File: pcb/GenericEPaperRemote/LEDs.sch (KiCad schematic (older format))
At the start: 26 parts

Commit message: Added pullups for encoder and switch away from io0 to prevent boot to root-loader when rotary encoder pulls low)
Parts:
- D17, D18, D19, D20, D21, D22, D23, D24, D25, D26, D27, D28, D29: LCSC Url https://lcsc.com/product-detail/New-Arrivals_JST-Sales-Amer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 -> https://lcsc.com/product-detail/Light-Emitting-Diodes-LED_5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
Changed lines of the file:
@@
 F 2 "LED_SMD:LED_WS2812B_PLCC4_5.0x5.0mm_P3.2mm" H 1900 1850 50  0001 L TNN
 F 3 "https://cdn-shop.adafruit.com/datasheets/WS2812B.pdf" H 1950 1775 50  0001 L TNN
-F 4 "https://lcsc.com/product-detail/New-Arrivals_JST-Sales-America-S8B-PH-SM4-TB-LF-SN_C265121.html" H 1850 2150 50  0001 C CNN "LCSC Url"
+F 4 "https://lcsc.com/product-detail/Light-Emitting-Diodes-LED_5050-RGBIntegrated-Light-4Pin_C114586.html" H 1850 2150 50  0001 C CNN "LCSC Url"
 F 5 "WS2812B-B" H 1850 2150 50  0001 C CNN "MPN"
 	1    1850 2150
@@
 F 2 "LED_SMD:LED_WS2812B_PLCC4_5.0x5.0mm_P3.2mm" H 2500 1850 50  0001 L TNN
 F 3 "https://cdn-shop.adafruit.com/datasheets/WS2812B.pdf" H 2550 1775 50  0001 L TNN
-F 4 "https://lcsc.com/product-detail/New-Arrivals_JST-Sales-America-S8B-PH-SM4-TB-LF-SN_C265121.html" H 2450 2150 50  0001 C CNN "LCSC Url"
+F 4 "https://lcsc.com/product-detail/Light-Emitting-Diodes-LED_5050-RGBIntegrated-Light-4Pin_C114586.html" H 2450 2150 50  0001 C CNN "LCSC Url"
 F 5 "WS2812B-B" H 2450 2150 50  0001 C CNN "MPN"
 	1    2450 2150
@@
 F 2 "LED_SMD:LED_WS2812B_PLCC4_5.0x5.0mm_P3.2mm" H 3100 1850 50  0001 L TNN
 F 3 "https://cdn-shop.adafruit.com/datasheets/WS2812B.pdf" H 3150 1775 50  0001 L TNN
-F 4 "https://lcsc.com/product-detail/New-Arrivals_JST-Sales-America-S8B-PH-SM4-TB-LF-SN_C265121.html" H 3050 2150 50  0001 C CNN "LCSC Url"
+F 4 "https://lcsc.com/product-detail/Light-Emitting-Diodes-LED_5050-RGBIntegrated-Light-4Pin_C114586.html" H 3050 2150 50  0001 C CNN "LCSC Url"
 F 5 "WS2812B-B" H 3050 2150 50  0001 C CNN "MPN"
 	1    3050 2150
@@
 F 2 "LED_SMD:LED_WS2812B_PLCC4_5.0x5.0mm_P3.2mm" H 3700 1850 50  0001 L TNN
 F 3 "https://cdn-shop.adafruit.com/datasheets/WS2812B.pdf" H 3750 1775 50  0001 L TNN
-F 4 "https://lcsc.com/product-detail/New-Arrivals_JST-Sales-America-S8B-PH-SM4-TB-LF-SN_C265121.html" H 3650 2150 50  0001 C CNN "LCSC Url"
+F 4 "https://lcsc.com/product-detail/Light-Emitting-Diodes-LED_5050-RGBIntegrated-Light-4Pin_C114586.html" H 3650 2150 50  0001 C CNN "LCSC Url"
 F 5 "WS2812B-B" H 3650 2150 50  0001 C CNN "MPN"
 	1    3650 2150
@@
 F 2 "LED_SMD:LED_WS2812B_PLCC4_5.0x5.0mm_P3.2mm" H 4300 1850 50  0001 L TNN
 F 3 "https://cdn-shop.adafruit.com/datasheets/WS2812B.pdf" H 4350 1775 50  0001 L TNN
-F 4 "https://lcsc.com/product-detail/New-Arrivals_JST-Sales-America-S8B-PH-SM4-TB-LF-SN_C265121.html" H 4250 2150 50  0001 C CNN "LCSC Url"
+F 4 "https://lcsc.com/product-detail/Light-Emitting-Diodes-LED_5050-RGBIntegrated-Light-4Pin_C114586.html" H 4250 2150 50  0001 C CNN "LCSC Url"
 F 5 "WS2812B-B" H 4250 2150 50  0001 C CNN "MPN"
 	1    4250 2150
@@
 F 2 "LED_SMD:LED_WS2812B_PLCC4_5.0x5.0mm_P3.2mm" H 4900 1850 50  0001 L TNN
 F 3 "https://cdn-shop.adafruit.com/datasheets/WS2812B.pdf" H 4950 1775 50  0001 L TNN
-F 4 "https://lcsc.com/product-detail/New-Arrivals_JST-Sales-America-S8B-PH-SM4-TB-LF-SN_C265121.html" H 4850 2150 50  0001 C CNN "LCSC Url"
+F 4 "https://lcsc.com/product-detail/Light-Emitting-Diodes-LED_5050-RGBIntegrated-Light-4Pin_C114586.html" H 4850 2150 50  0001 C CNN "LCSC Url"
 F 5 "WS2812B-B" H 4850 2150 50  0001 C CNN "MPN"
 	1    4850 2150
@@
 F 2 "LED_SMD:LED_WS2812B_PLCC4_5.0x5.0mm_P3.2mm" H 5500 1850 50  0001 L TNN
 F 3 "https://cdn-shop.adafruit.com/datasheets/WS2812B.pdf" H 5550 1775 50  0001 L TNN
-F 4 "https://lcsc.com/product-detail/New-Arrivals_JST-Sales-America-S8B-PH-SM4-TB-LF-SN_C265121.html" H 5450 2150 50  0001 C CNN "LCSC Url"
+F 4 "https://lcsc.com/product-detail/Light-Emitting-Diodes-LED_5050-RGBIntegrated-Light-4Pin_C114586.html" H 5450 2150 50  0001 C CNN "LCSC Url"
 F 5 "WS2812B-B" H 5450 2150 50  0001 C CNN "MPN"
 	1    5450 2150
@@
 F 2 "LED_SMD:LED_WS2812B_PLCC4_5.0x5.0mm_P3.2mm" H 6100 1850 50  0001 L TNN
 F 3 "https://cdn-shop.adafruit.com/datasheets/WS2812B.pdf" H 6150 1775 50  0001 L TNN
-F 4 "https://lcsc.com/product-detail/New-Arrivals_JST-Sales-America-S8B-PH-SM4-TB-LF-SN_C265121.html" H 6050 2150 50  0001 C CNN "LCSC Url"
+F 4 "https://lcsc.com/product-detail/Light-Emitting-Diodes-LED_5050-RGBIntegrated-Light-4Pin_C114586.html" H 6050 2150 50  0001 C CNN "LCSC Url"
 F 5 "WS2812B-B" H 6050 2150 50  0001 C CNN "MPN"
 	1    6050 2150
@@
 F 2 "LED_SMD:LED_WS2812B_PLCC4_5.0x5.0mm_P3.2mm" H 6700 1850 50  0001 L TNN
 F 3 "https://cdn-shop.adafruit.com/datasheets/WS2812B.pdf" H 6750 1775 50  0001 L TNN
-F 4 "https://lcsc.com/product-detail/New-Arrivals_JST-Sales-America-S8B-PH-SM4-TB-LF-SN_C265121.html" H 6650 2150 50  0001 C CNN "LCSC Url"
+F 4 "https://lcsc.com/product-detail/Light-Emitting-Diodes-LED_5050-RGBIntegrated-Light-4Pin_C114586.html" H 6650 2150 50  0001 C CNN "LCSC Url"
 F 5 "WS2812B-B" H 6650 2150 50  0001 C CNN "MPN"
 	1    6650 2150
@@
 F 2 "LED_SMD:LED_WS2812B_PLCC4_5.0x5.0mm_P3.2mm" H 7300 1850 50  0001 L TNN
 F 3 "https://cdn-shop.adafruit.com/datasheets/WS2812B.pdf" H 7350 1775 50  0001 L TNN
-F 4 "https://lcsc.com/product-detail/New-Arrivals_JST-Sales-America-S8B-PH-SM4-TB-LF-SN_C265121.html" H 7250 2150 50  0001 C CNN "LCSC Url"
+F 4 "https://lcsc.com/product-detail/Light-Emitting-Diodes-LED_5050-RGBIntegrated-Light-4Pin_C114586.html" H 7250 2150 50  0001 C CNN "LCSC Url"
 F 5 "WS2812B-B" H 7250 2150 50  0001 C CNN "MPN"
 	1    7250 2150
@@
 F 2 "LED_SMD:LED_WS2812B_PLCC4_5.0x5.0mm_P3.2mm" H 7900 1850 50  0001 L TNN
 F 3 "https://cdn-shop.adafruit.com/datasheets/WS2812B.pdf" H 7950 1775 50  0001 L TNN
-F 4 "https://lcsc.com/product-detail/New-Arrivals_JST-Sales-America-S8B-PH-SM4-TB-LF-SN_C265121.html" H 7850 2150 50  0001 C CNN "LCSC Url"
+F 4 "https://lcsc.com/product-detail/Light-Emitting-Diodes-LED_5050-RGBIntegrated-Light-4Pin_C114586.html" H 7850 2150 50  0001 C CNN "LCSC Url"
 F 5 "WS2812B-B" H 7850 2150 50  0001 C CNN "MPN"
 	1    7850 2150
@@
 F 2 "LED_SMD:LED_WS2812B_PLCC4_5.0x5.0mm_P3.2mm" H 8500 1850 50  0001 L TNN
 F 3 "https://cdn-shop.adafruit.com/datasheets/WS2812B.pdf" H 8550 1775 50  0001 L TNN
-F 4 "https://lcsc.com/product-detail/New-Arrivals_JST-Sales-America-S8B-PH-SM4-TB-LF-SN_C265121.html" H 8450 2150 50  0001 C CNN "LCSC Url"
+F 4 "https://lcsc.com/product-detail/Light-Emitting-Diodes-LED_5050-RGBIntegrated-Light-4Pin_C114586.html" H 8450 2150 50  0001 C CNN "LCSC Url"
 F 5 "WS2812B-B" H 8450 2150 50  0001 C CNN "MPN"
 	1    8450 2150
@@
 F 2 "LED_SMD:LED_WS2812B_PLCC4_5.0x5.0mm_P3.2mm" H 9100 1850 50  0001 L TNN
 F 3 "https://cdn-shop.adafruit.com/datasheets/WS2812B.pdf" H 9150 1775 50  0001 L TNN
-F 4 "https://lcsc.com/product-detail/New-Arrivals_JST-Sales-America-S8B-PH-SM4-TB-LF-SN_C265121.html" H 9050 2150 50  0001 C CNN "LCSC Url"
+F 4 "https://lcsc.com/product-detail/Light-Emitting-Diodes-LED_5050-RGBIntegrated-Light-4Pin_C114586.html" H 9050 2150 50  0001 C CNN "LCSC Url"
 F 5 "WS2812B-B" H 9050 2150 50  0001 C CNN "MPN"
 	1    9050 2150

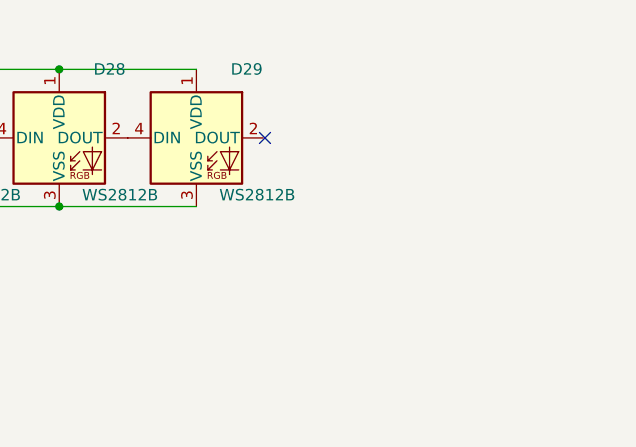
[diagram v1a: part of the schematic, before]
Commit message: added extension pins for ws2812b
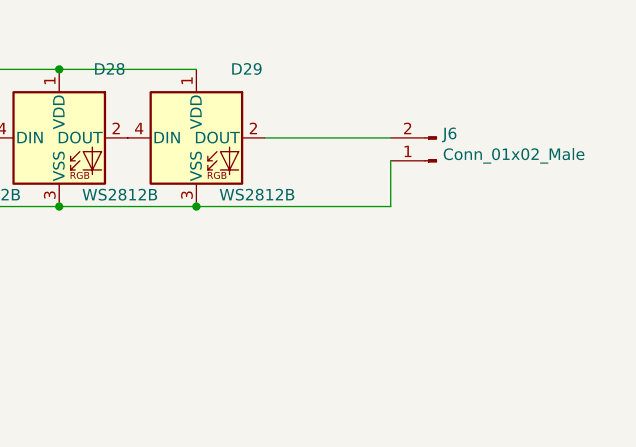
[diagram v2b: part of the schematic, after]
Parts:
- added J6: Conn_01x02_Male, Connector_PinHeader_2.54mm:PinHeader_1x02_P2.54mm_Vertical, symbol Connector:Conn_01x02_Male
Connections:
- net GND: now also J6.1 (Pin_1)
- net at D29.2 (DOUT): now also J6.2 (Pin_2)
- no-connect marks 1 -> 0
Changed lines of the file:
@@
 Wire Wire Line
 	5950 3400 5550 3400
-NoConn ~ 9350 2150
+$Comp
+L Connector:Conn_01x02_Male J6
+U 1 1 5FC563AD
+P 10100 2250
+F 0 "J6" H 10072 2132 50  0000 R CNN
+F 1 "Conn_01x02_Male" H 10072 2223 50  0000 R CNN
+F 2 "Connector_PinHeader_2.54mm:PinHeader_1x02_P2.54mm_Vertical" H 10100 2250 50  0001 C CNN
+F 3 "~" H 10100 2250 50  0001 C CNN
+	1    10100 2250
+	-1   0    0    1
+$EndComp
+Wire Wire Line
+	9350 2150 9900 2150
+Wire Wire Line
+	9050 2450 9900 2450
+Wire Wire Line
+	9900 2450 9900 2250
+Connection ~ 9050 2450
 $EndSCHEMATC
